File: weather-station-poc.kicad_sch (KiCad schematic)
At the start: 0 parts

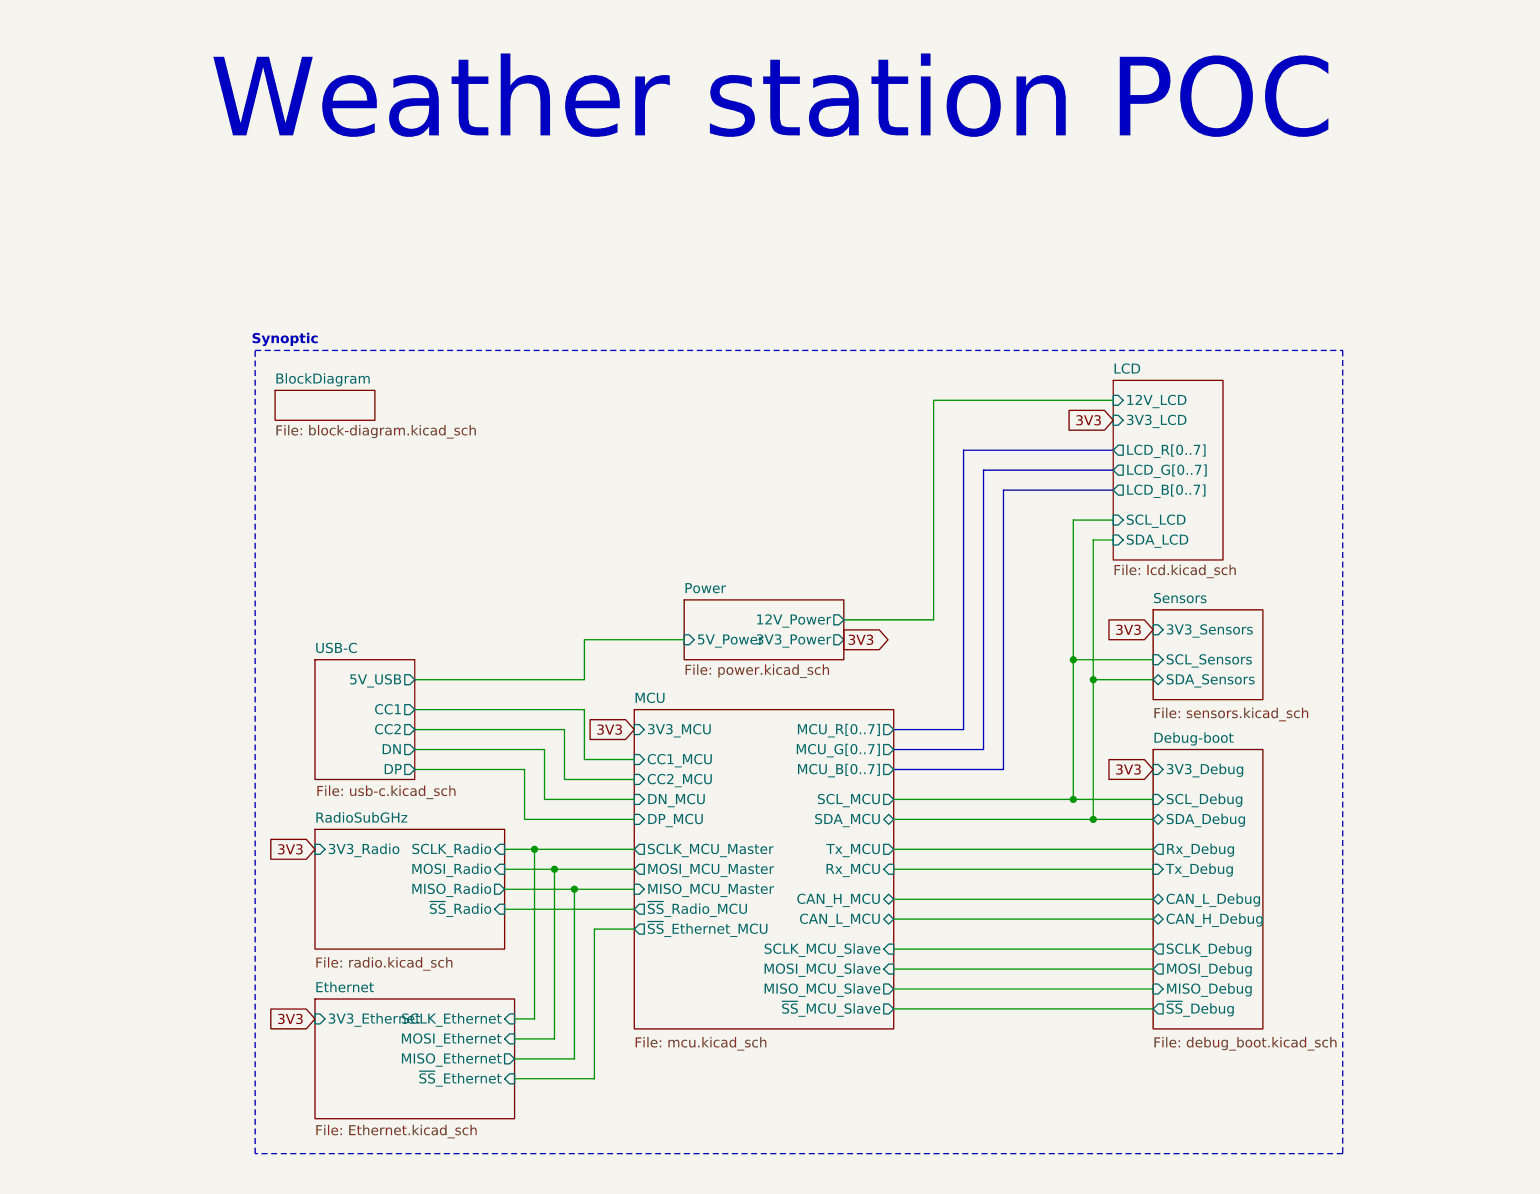
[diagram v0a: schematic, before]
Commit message: Add WLED driver in power shcematic
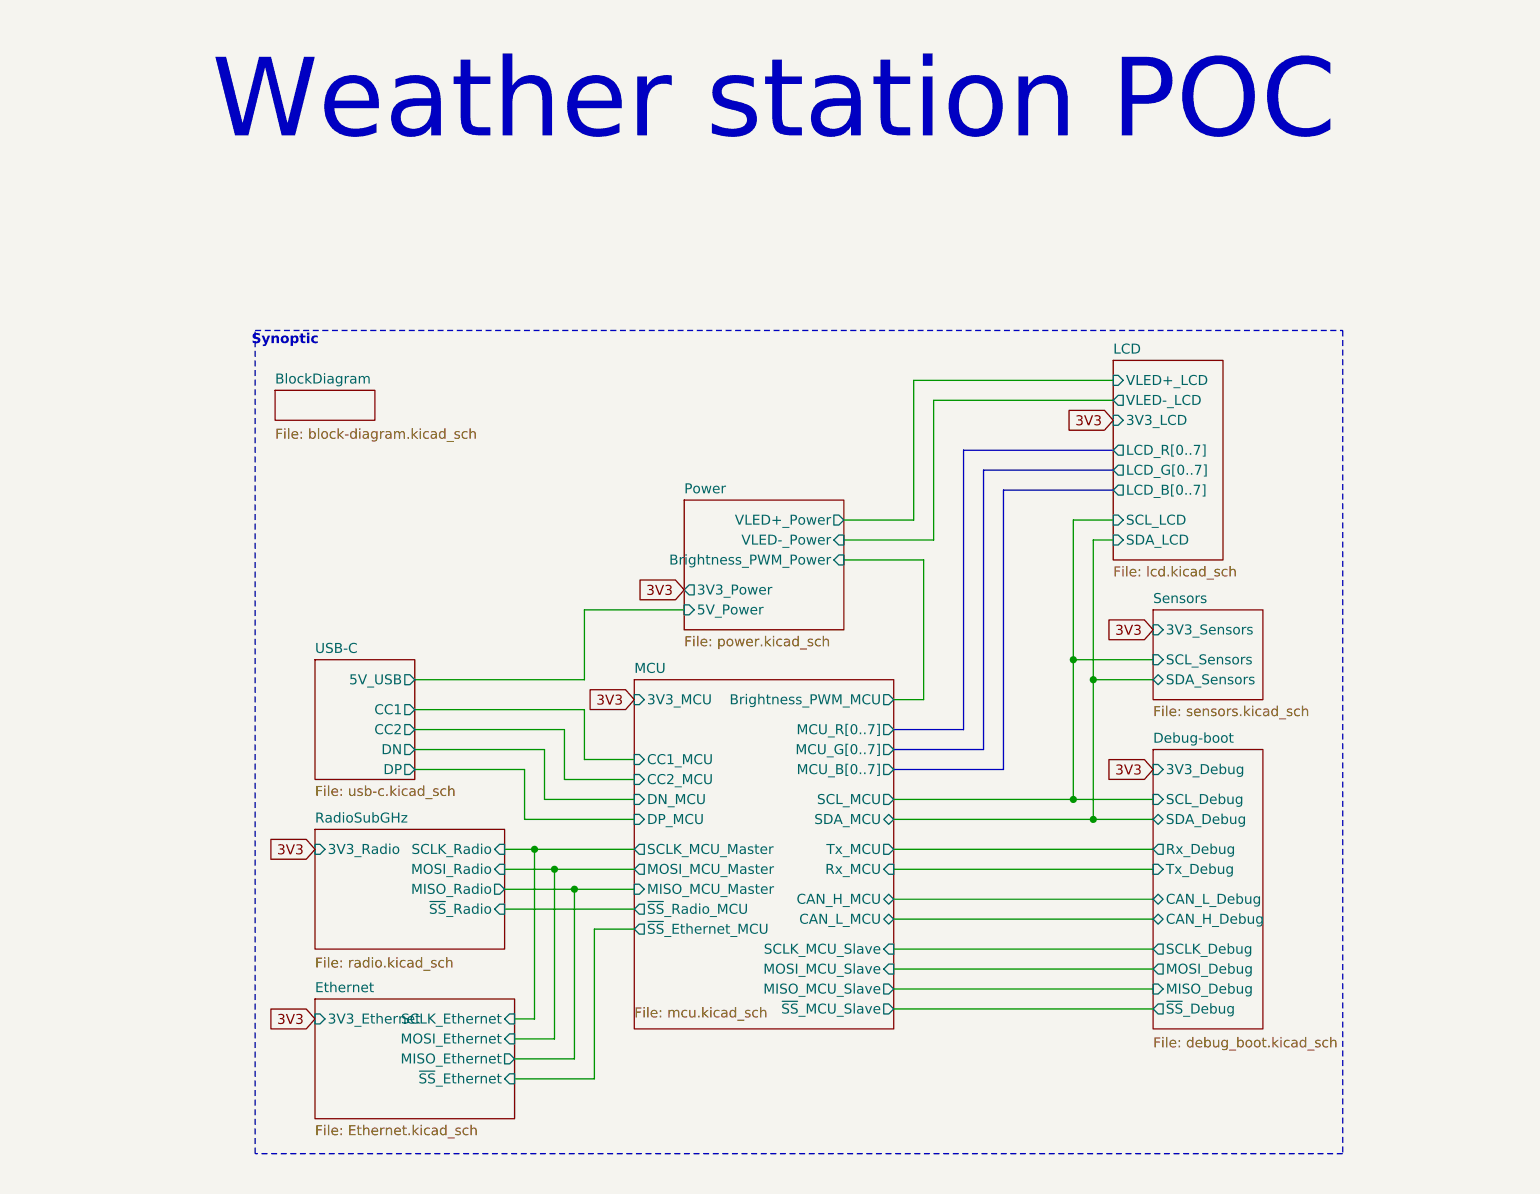
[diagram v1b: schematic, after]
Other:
- sheet LCD ports: added VLED+_LCD, VLED-_LCD; removed 12V_LCD
- sheet MCU ports: added Brightness_PWM_MCU; removed none
- sheet Power ports: added Brightness_PWM_Power, VLED+_Power, VLED-_Power; removed 12V_Power
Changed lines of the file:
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@@
 	)
 	(rectangle
-		(start 83.82 55.88)
+		(start 83.82 53.34)
 		(end 222.25 158.115)
 		(stroke
@@
 	(text "Weather station POC"
 		(exclude_from_sim no)
-		(at 149.606 24.13 0)
+		(at 149.86 24.13 0)
 		(effects
 			(font
@@
 	(wire
 		(pts
+			(xy 167.64 77.47) (xy 167.64 59.69)
+		)
+		(stroke
+			(width 0)
+			(type default)
+		)
+	)
+	(wire
+		(pts
 			(xy 124.46 146.05) (xy 116.84 146.05)
 		)
@@
 	(wire
 		(pts
+			(xy 165.1 100.33) (xy 168.91 100.33)
+		)
+		(stroke
+			(width 0)
+			(type default)
+		)
+	)
+	(wire
+		(pts
 			(xy 190.5 97.79) (xy 198.12 97.79)
 		)
@@
 	(wire
 		(pts
+			(xy 170.18 80.01) (xy 170.18 62.23)
+		)
+		(stroke
+			(width 0)
+			(type default)
+		)
+	)
+	(wire
+		(pts
 			(xy 190.5 80.01) (xy 193.04 80.01)
 		)
@@
 	(wire
 		(pts
+			(xy 167.64 59.69) (xy 193.04 59.69)
+		)
+		(stroke
+			(width 0)
+			(type default)
+		)
+	)
+	(wire
+		(pts
 			(xy 198.12 95.25) (xy 187.96 95.25)
 		)
@@
 	(wire
 		(pts
+			(xy 158.75 77.47) (xy 167.64 77.47)
+		)
+		(stroke
+			(width 0)
+			(type default)
+		)
+	)
+	(wire
+		(pts
 			(xy 165.1 125.73) (xy 198.12 125.73)
 		)
@@
 	(wire
 		(pts
+			(xy 170.18 62.23) (xy 193.04 62.23)
+		)
+		(stroke
+			(width 0)
+			(type default)
+		)
+	)
+	(wire
+		(pts
 			(xy 120.65 113.03) (xy 132.08 113.03)
 		)
@@
 	(wire
 		(pts
+			(xy 168.91 82.55) (xy 158.75 82.55)
+		)
+		(stroke
+			(width 0)
+			(type default)
+		)
+	)
+	(wire
+		(pts
 			(xy 132.08 129.54) (xy 127 129.54)
 		)
@@
 	(wire
 		(pts
-			(xy 158.75 90.17) (xy 170.18 90.17)
-		)
-		(stroke
-			(width 0)
-			(type default)
-		)
-	)
-	(wire
-		(pts
 			(xy 119.38 140.97) (xy 116.84 140.97)
 		)
@@
 	(wire
 		(pts
-			(xy 125.73 97.79) (xy 125.73 92.71)
+			(xy 125.73 97.79) (xy 125.73 88.9)
 		)
 		(stroke
@@
 	(wire
 		(pts
-			(xy 170.18 62.23) (xy 193.04 62.23)
-		)
-		(stroke
-			(width 0)
-			(type default)
-		)
-	)
-	(wire
-		(pts
-			(xy 125.73 92.71) (xy 138.43 92.71)
+			(xy 125.73 88.9) (xy 138.43 88.9)
 		)
 		(stroke
@@
 	(wire
 		(pts
-			(xy 170.18 90.17) (xy 170.18 62.23)
+			(xy 168.91 100.33) (xy 168.91 82.55)
+		)
+		(stroke
+			(width 0)
+			(type default)
+		)
+	)
+	(wire
+		(pts
+			(xy 158.75 80.01) (xy 170.18 80.01)
 		)
 		(stroke
@@
 	)
 	(global_label "3V3"
-		(shape output)
-		(at 158.75 92.71 0)
+		(shape input)
+		(at 132.08 100.33 180)
 		(fields_autoplaced yes)
 		(effects
@@
 				(size 1.27 1.27)
 			)
-			(justify left)
+			(justify right)
 		)
 		(property "Intersheetrefs" "${INTERSHEET_REFS}"
-			(at 164.3231 92.71 0)
-			(effects
-				(font
-					(size 1.27 1.27)
-				)
-				(justify left)
-				(hide yes)
-			)
-		)
-	)
-	(global_label "3V3"
-		(shape input)
-		(at 132.08 104.14 180)
-		(fields_autoplaced yes)
-		(effects
-			(font
-				(size 1.27 1.27)
-			)
-			(justify right)
-		)
-		(property "Intersheetrefs" "${INTERSHEET_REFS}"
-			(at 126.5069 104.14 0)
+			(at 126.5069 100.33 0)
 			(effects
 				(font
@@
 		)
 	)
+	(global_label "3V3"
+		(shape input)
+		(at 138.43 86.36 180)
+		(fields_autoplaced yes)
+		(effects
+			(font
+				(size 1.27 1.27)
+			)
+			(justify right)
+		)
+		(property "Intersheetrefs" "${INTERSHEET_REFS}"
+			(at 132.8569 86.36 0)
+			(effects
+				(font
+					(size 1.27 1.27)
+				)
+				(justify right)
+				(hide yes)
+			)
+		)
+	)
 	(sheet
-		(at 138.43 87.63)
-		(size 20.32 7.62)
+		(at 138.43 74.93)
+		(size 20.32 16.51)
 		(exclude_from_sim no)
 		(in_bom yes)
 		(on_board yes)
 		(dnp no)
-		(fields_autoplaced yes)
 		(stroke
 			(width 0.1524)
@@
 		)
 		(property "Sheetname" "Power"
-			(at 138.43 86.9184 0)
+			(at 138.43 74.2184 0)
 			(effects
 				(font
@@
 		)
 		(property "Sheetfile" "power.kicad_sch"
-			(at 138.43 95.8346 0)
+			(at 138.43 92.202 0)
 			(effects
 				(font
@@
 		)
 		(pin "3V3_Power" output
-			(at 158.75 92.71 0)
-			(effects
-				(font
-					(size 1.27 1.27)
-				)
-				(justify right)
+			(at 138.43 86.36 180)
+			(effects
+				(font
+					(size 1.27 1.27)
+				)
+				(justify left)
 			)
 		)
 		(pin "5V_Power" input
-			(at 138.43 92.71 180)
-			(effects
-				(font
-					(size 1.27 1.27)
-				)
-				(justify left)
-			)
-		)
-		(pin "12V_Power" output
-			(at 158.75 90.17 0)
+			(at 138.43 88.9 180)
+			(effects
+				(font
+					(size 1.27 1.27)
+				)
+				(justify left)
+			)
+		)
+		(pin "VLED+_Power" output
+			(at 158.75 77.47 0)
+			(effects
+				(font
+					(size 1.27 1.27)
+				)
+				(justify right)
+			)
+		)
+		(pin "VLED-_Power" input
+			(at 158.75 80.01 0)
+			(effects
+				(font
+					(size 1.27 1.27)
+				)
+				(justify right)
+			)
+		)
+		(pin "Brightness_PWM_Power" input
+			(at 158.75 82.55 0)
 			(effects
 				(font
@@
 		)
 		(property "Sheetfile" "sensors.kicad_sch"
-			(at 198.12 101.346 0)
+			(at 198.12 101.092 0)
 			(effects
 				(font
@@
 		)
 		(property "Sheetfile" "usb-c.kicad_sch"
-			(at 91.567 111.252 0)
+			(at 91.44 111.252 0)
 			(effects
 				(font
@@
 	)
 	(sheet
-		(at 132.08 101.6)
-		(size 33.02 40.64)
+		(at 132.08 97.79)
+		(size 33.02 44.45)
 		(exclude_from_sim no)
 		(in_bom yes)
@@
 		)
 		(property "Sheetname" "MCU"
-			(at 132.08 100.8884 0)
+			(at 132.08 97.0784 0)
 			(effects
 				(font
@@
 		)
 		(property "Sheetfile" "mcu.kicad_sch"
-			(at 132.08 143.256 0)
+			(at 132.08 139.446 0)
 			(effects
 				(font
@@
 		)
 		(pin "3V3_MCU" input
-			(at 132.08 104.14 180)
+			(at 132.08 100.33 180)
 			(effects
 				(font
@@
 		(pin "MCU_B[0..7]" output
 			(at 165.1 109.22 0)
+			(effects
+				(font
+					(size 1.27 1.27)
+				)
+				(justify right)
+			)
+		)
+		(pin "Brightness_PWM_MCU" output
+			(at 165.1 100.33 0)
 			(effects
 				(font
@@
 	)
 	(sheet
-		(at 193.04 59.69)
-		(size 13.97 22.86)
+		(at 193.04 57.15)
+		(size 13.97 25.4)
 		(exclude_from_sim no)
 		(in_bom yes)
 		(on_board yes)
 		(dnp no)
-		(fields_autoplaced yes)
 		(stroke
 			(width 0.1524)
@@
 		)
 		(property "Sheetname" "LCD"
-			(at 193.04 58.9784 0)
+			(at 193.04 56.4384 0)
 			(effects
 				(font
@@
 		)
 		(property "Sheetfile" "lcd.kicad_sch"
-			(at 193.04 83.1346 0)
+			(at 193.04 83.312 0)
 			(effects
 				(font
@@
 			)
 		)
-		(pin "12V_LCD" input
-			(at 193.04 62.23 180)
-			(effects
-				(font
-					(size 1.27 1.27)
-				)
-				(justify left)
-			)
-		)
 		(pin "SCL_LCD" input
 			(at 193.04 77.47 180)
@@
 		(pin "LCD_G[0..7]" output
 			(at 193.04 71.12 180)
+			(effects
+				(font
+					(size 1.27 1.27)
+				)
+				(justify left)
+			)
+		)
+		(pin "VLED+_LCD" input
+			(at 193.04 59.69 180)
+			(effects
+				(font
+					(size 1.27 1.27)
+				)
+				(justify left)
+			)
+		)
+		(pin "VLED-_LCD" output
+			(at 193.04 62.23 180)
 			(effects
 				(font
@@
 		(on_board yes)
 		(dnp no)
-		(fields_autoplaced yes)
 		(stroke
 			(width 0.1524)
@@
 		)
 		(property "Sheetfile" "block-diagram.kicad_sch"
-			(at 86.36 65.3546 0)
-			(effects
-				(font
+			(at 86.36 65.786 0)
+			(effects
+				(font

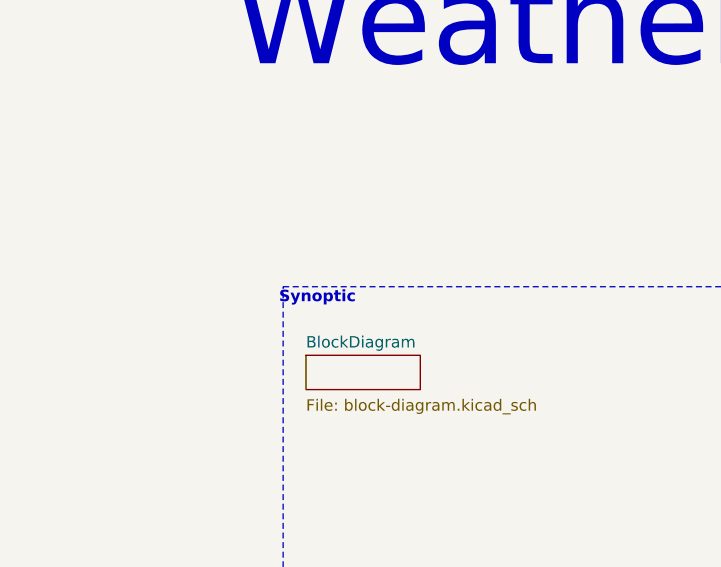
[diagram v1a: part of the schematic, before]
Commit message: Add FPC/FFC connectors for LCD display screen
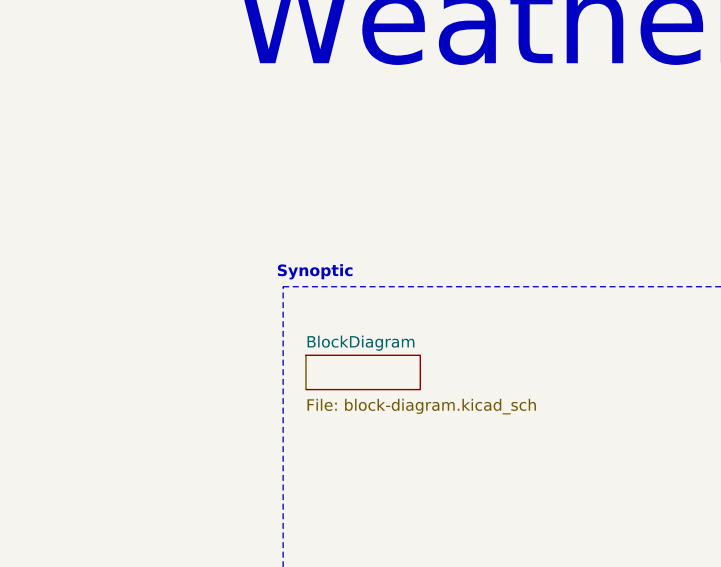
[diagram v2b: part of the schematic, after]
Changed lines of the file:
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@@
 	(text "Synoptic"
 		(exclude_from_sim no)
-		(at 87.63 54.61 0)
+		(at 87.376 51.816 0)
 		(effects
 			(font

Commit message: Synchronise hierarchical pins for LCD
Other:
- sheet LCD ports: added DCLK_LCD, DE_LCD, DISP_LCD, HSYNC_LCD, I2C_INT_LCD, I2C_RST_LCD, VSYNC_LCD; removed none
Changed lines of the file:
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@@
 	(sheet
 		(at 193.04 57.15)
-		(size 13.97 25.4)
+		(size 24.13 25.4)
 		(exclude_from_sim no)
 		(in_bom yes)
@@
 			)
 		)
+		(pin "DCLK_LCD" input
+			(at 217.17 59.69 0)
+			(effects
+				(font
+					(size 1.27 1.27)
+				)
+				(justify right)
+			)
+		)
+		(pin "DISP_LCD" input
+			(at 217.17 62.23 0)
+			(effects
+				(font
+					(size 1.27 1.27)
+				)
+				(justify right)
+			)
+		)
+		(pin "DE_LCD" input
+			(at 217.17 64.77 0)
+			(effects
+				(font
+					(size 1.27 1.27)
+				)
+				(justify right)
+			)
+		)
+		(pin "HSYNC_LCD" input
+			(at 217.17 67.31 0)
+			(effects
+				(font
+					(size 1.27 1.27)
+				)
+				(justify right)
+			)
+		)
+		(pin "VSYNC_LCD" input
+			(at 217.17 69.85 0)
+			(effects
+				(font
+					(size 1.27 1.27)
+				)
+				(justify right)
+			)
+		)
+		(pin "I2C_RST_LCD" input
+			(at 217.17 72.39 0)
+			(effects
+				(font
+					(size 1.27 1.27)
+				)
+				(justify right)
+			)
+		)
+		(pin "I2C_INT_LCD" output
+			(at 217.17 74.93 0)
+			(effects
+				(font
+					(size 1.27 1.27)
+				)
+				(justify right)
+			)
+		)
